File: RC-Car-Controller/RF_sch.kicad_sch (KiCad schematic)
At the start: 13 parts, among them U1 AT86RF215-ZU, U5 RFX2401C, U6 2450FB15A050E

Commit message: Fixed Controller PCB
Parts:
- C24, C25, C26, C27, C28, C29, C30, C31, C32, C33: footprint (none) -> Capacitor_SMD:C_0201_0603Metric
- U1: footprint QFN48_PQ_MCH -> footprints:QFN48_PQ_MCH
- U5: footprint RFX2401C_SKY -> footprints:RFX2401C_SKY
- U6: footprint 2450FB15A050E_JOT -> footprints:2450FB15A050E_JOT
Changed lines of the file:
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@@
 			)
 		)
-		(property "Footprint" "QFN48_PQ_MCH"
+		(property "Footprint" "footprints:QFN48_PQ_MCH"
 			(at 105.41 128.27 0)
 			(effects
@@
 			)
 		)
-		(property "Footprint" ""
+		(property "Footprint" "Capacitor_SMD:C_0201_0603Metric"
 			(at 267.6652 100.33 0)
 			(effects
@@
 			)
 		)
-		(property "Footprint" ""
+		(property "Footprint" "Capacitor_SMD:C_0201_0603Metric"
 			(at 101.2952 156.21 0)
 			(effects
@@
 			)
 		)
-		(property "Footprint" ""
+		(property "Footprint" "Capacitor_SMD:C_0201_0603Metric"
 			(at 59.3852 156.21 0)
 			(effects
@@
 			)
 		)
-		(property "Footprint" ""
+		(property "Footprint" "Capacitor_SMD:C_0201_0603Metric"
 			(at 77.1652 156.21 0)
 			(effects
@@
 			)
 		)
-		(property "Footprint" ""
+		(property "Footprint" "Capacitor_SMD:C_0201_0603Metric"
 			(at 93.6752 156.21 0)
 			(effects
@@
 			)
 		)
-		(property "Footprint" ""
+		(property "Footprint" "Capacitor_SMD:C_0201_0603Metric"
 			(at 108.9152 156.21 0)
 			(effects
@@
 			)
 		)
-		(property "Footprint" ""
+		(property "Footprint" "Capacitor_SMD:C_0201_0603Metric"
 			(at 271.4752 95.25 0)
 			(effects
@@
 			)
 		)
-		(property "Footprint" ""
+		(property "Footprint" "Capacitor_SMD:C_0201_0603Metric"
 			(at 86.0552 156.21 0)
 			(effects
@@
 			)
 		)
-		(property "Footprint" ""
+		(property "Footprint" "Capacitor_SMD:C_0201_0603Metric"
 			(at 68.2752 156.21 0)
 			(effects
@@
 			)
 		)
-		(property "Footprint" ""
+		(property "Footprint" "Capacitor_SMD:C_0201_0603Metric"
 			(at 50.4952 156.21 0)
 			(effects
@@
 			)
 		)
-		(property "Footprint" "2450FB15A050E_JOT"
+		(property "Footprint" "footprints:2450FB15A050E_JOT"
 			(at 121.92 87.63 0)
 			(effects
@@
 			)
 		)
-		(property "Footprint" "RFX2401C_SKY"
+		(property "Footprint" "footprints:RFX2401C_SKY"
 			(at 222.25 85.09 0)
 			(effects

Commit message: Did power schtuff
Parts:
- removed C24, C25, C26, C27, C28, C29, C30, C31, C32, C33: 0.1uF/10V, Capacitor_SMD:C_0201_0603Metric, symbol Device:C
- removed U1: AT86RF215-ZU, footprints:QFN48_PQ_MCH, symbol AT86RF215:AT86RF215-ZU
- removed U5: RFX2401C, footprints:RFX2401C_SKY, symbol RFX2401C:RFX2401C
- removed U6: 2450FB15A050E, footprints:2450FB15A050E_JOT, symbol 2450FB15A050E Balun:2450FB15A050E
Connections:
- no-connect marks 21 -> 0

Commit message: Added FGH100M footprint/schematic
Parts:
- added R26, R28, R29, R30, R31: 10k, Capacitor_SMD:C_0603_1608Metric, symbol Device:R
- added U3: ~, FGH100M:FGH100MABMD, symbol FGH100M:FGH100MABMD
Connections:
- new net +3V3: R26.2, R28.2, R29.2, R30.2, R31.2, U3.17 (VBAT), U3.22 (VDD_IO), U3.4 (VDD_FEM)
- new net GNDA: U3.1 (GND), U3.18 (GND), U3.2 (GND), U3.21 (GND), U3.3 (GND), U3.31 (GND), U3.38 (GND), U3.39 (GND), U3.5 (GND), U3.7 (GND)
- new net SDIO_CLK: U3.24 (SDIO_CLK)
- new net SDIO_CMD: R26.1, U3.23 (SDIO_CMD)
- new net SDIO_DATA0: R28.1, U3.25 (SDIO_DATA0)
- new net SDIO_DATA1: R29.1, U3.26 (SDIO_DATA1)
- new net SDIO_DATA2: R30.1, U3.19 (SDIO_DATA2)
- new net SDIO_DATA3: R31.1, U3.20 (SDIO_DATA3)
- no-connect marks 0 -> 12

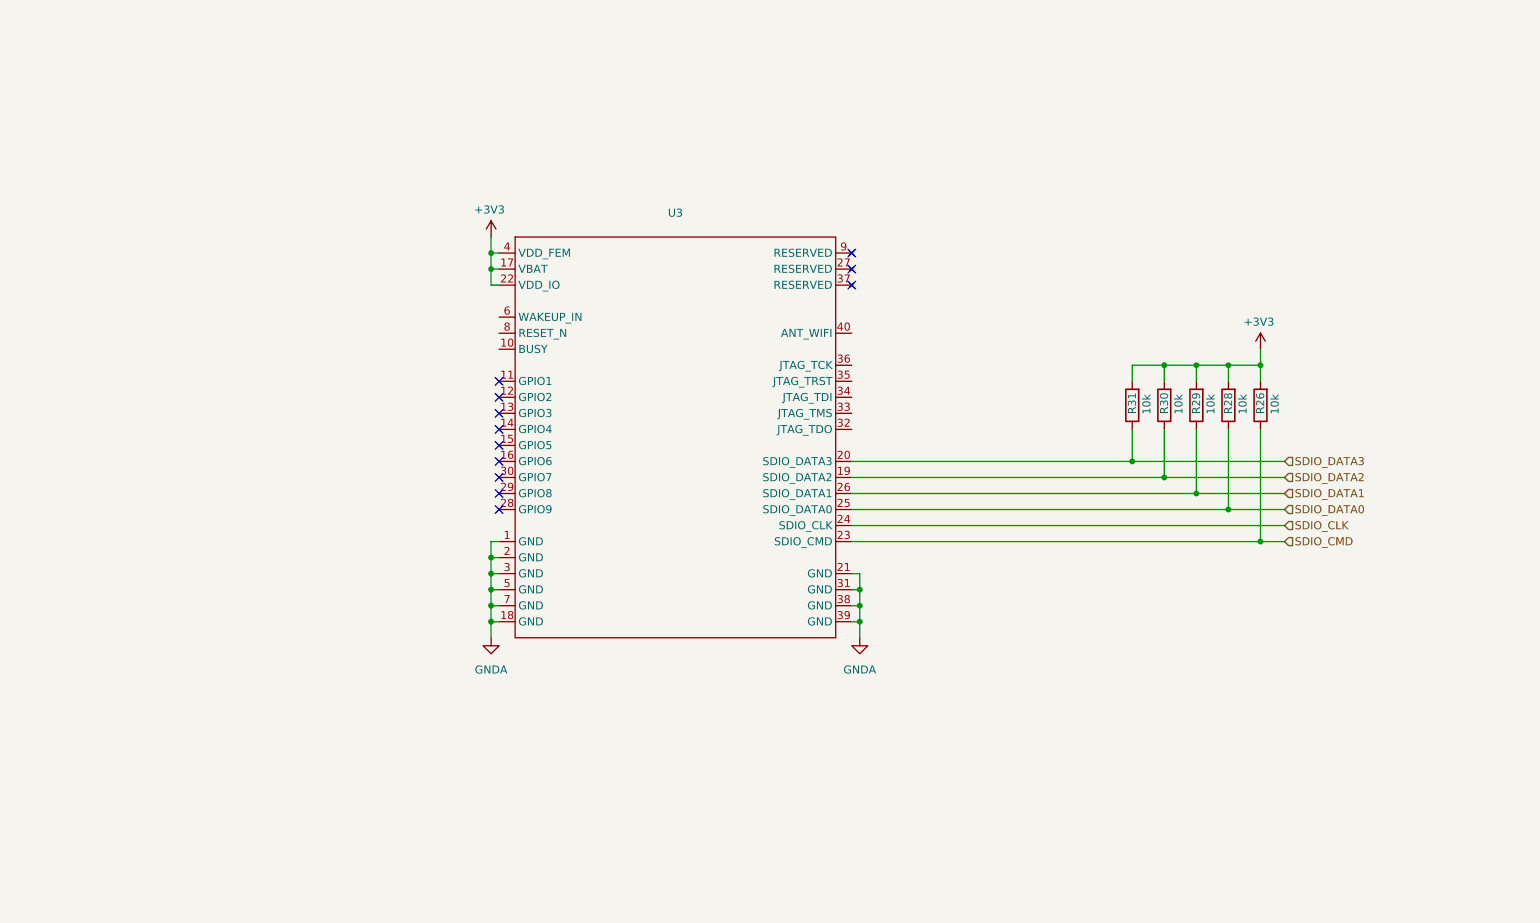
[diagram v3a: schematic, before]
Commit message: Wired up FGH100M
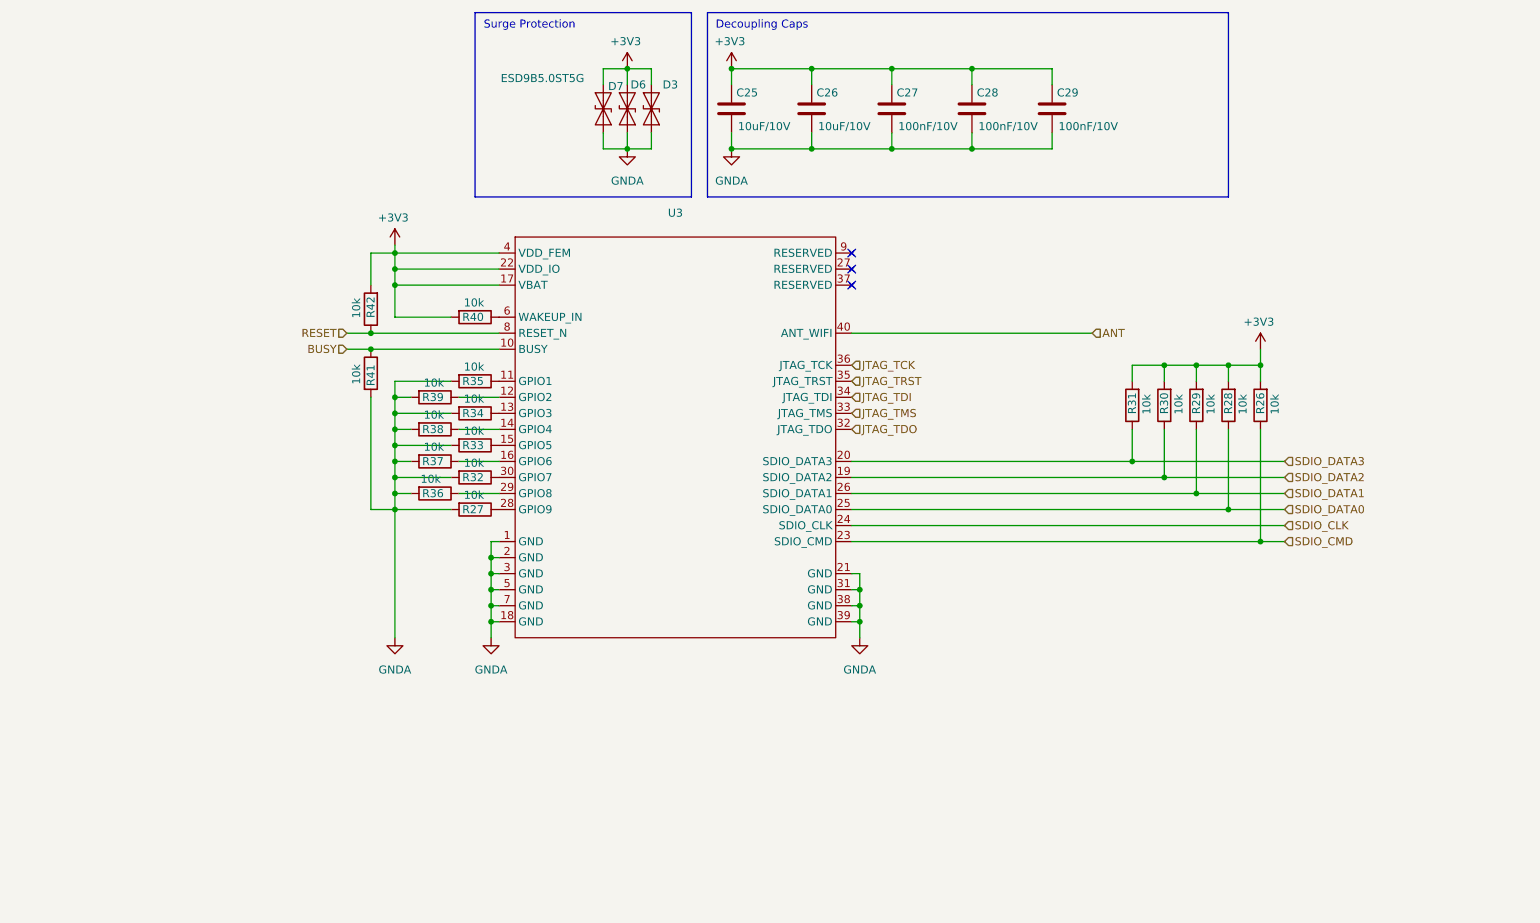
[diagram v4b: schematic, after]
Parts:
- added C25, C26: 10uF/10V, Capacitor_SMD:C_0603_1608Metric, symbol Device:C
- added C27, C28, C29: 100nF/10V, Capacitor_SMD:C_0603_1608Metric, symbol Device:C
- added D3, D6, D7: ESD9B5.0ST5G, Diode_SMD:D_SOD-923, symbol Diode:ESD9B5.0ST5G
- added R27, R32, R33, R34, R35, R36, R37, R38, R39, R40, R41, R42: 10k, Capacitor_SMD:C_0603_1608Metric, symbol Device:R
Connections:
- net +3V3: now also C25.1, C26.1, C27.1, C28.1, C29.1, D3.2 (A2), D6.2 (A2), D7.2 (A2), R40.2, R42.2
- net GNDA: now also C25.2, C26.2, C27.2, C28.2, C29.2, D3.1 (A1), D6.1 (A1), D7.1 (A1), R27.2, R32.2, R33.2, R34.2, R35.2, R36.2, R37.2, R38.2, R39.2, R41.2
- net BUSY: now reaches U3.10 (BUSY)
- net BUSY: now also R41.1
- net at U3.11 (GPIO1): now also R35.1
- net at U3.12 (GPIO2): now also R39.1
- net at U3.13 (GPIO3): now also R34.1
- net at U3.14 (GPIO4): now also R38.1
- net at U3.15 (GPIO5): now also R33.1
- net at U3.16 (GPIO6): now also R37.1
- net at U3.28 (GPIO9): now also R27.1
- net at U3.29 (GPIO8): now also R36.1
- net at U3.30 (GPIO7): now also R32.1
- net JTAG_TDO: now reaches U3.32 (JTAG_TDO)
- net JTAG_TMS: now reaches U3.33 (JTAG_TMS)
- net JTAG_TDI: now reaches U3.34 (JTAG_TDI)
- net JTAG_TRST: now reaches U3.35 (JTAG_TRST)
- net JTAG_TCK: now reaches U3.36 (JTAG_TCK)
- net ANT: now reaches U3.40 (ANT_WIFI)
- net at U3.6 (WAKEUP_IN): now also R40.1
- net RESET: now reaches U3.8 (RESET_N)
- net RESET: now also R42.1
- no-connect marks 12 -> 3
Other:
- note added: "Decoupling Caps"
- note added: "Surge Protection"

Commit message: Finished Controller PCB Pre-Review
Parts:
- added C26, C28: DNP, Capacitor_SMD:C_0603_1608Metric, symbol Device:C
- added FB1: FerriteBead, Capacitor_SMD:C_0603_1608Metric, symbol Device:FerriteBead
- added R35, R36, R37, R39: 10k, Capacitor_SMD:C_0603_1608Metric, symbol Device:R
- added R38: 0ohm, Resistor_SMD:R_0603_1608Metric, symbol Device:R
- D6: renamed from D7; now not fitted; now left out of the parts list
- D7: renamed from D6; now not fitted; now left out of the parts list
- D8: renamed from D3; now not fitted; now left out of the parts list
- renumbered C26 to C23, C29 to C24, C28 to C25, C25 to C27, C27 to C29, R42 to R23, R41 to R24, R39 to R25, R38 to R26, R37 to R27, R36 to R28, R40 to R29, R35 to R30, R34 to R31, R33 to R32, R32 to R33, R27 to R34, R31 to R40, R30 to R41, R29 to R42, R28 to R43, R26 to R44, U3 to U6
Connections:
- net +3V3: now also FB1.1; no longer C27.1, C29.1, U6.4 (VDD_FEM)
- net ANT: now also C28.1, R38.1; no longer U6.40 (ANT_WIFI)
- net GNDA: now also C26.2, C28.2, R35.1, R36.1, R37.1, R39.1
- net JTAG_TCK: now also R39.2
- net JTAG_TDI: now also R37.2
- net JTAG_TDO: now also R35.2
- net JTAG_TMS: now also R36.2
- new net: C26.1, R38.2, U6.40 (ANT_WIFI)
- new net VDD_FEM: C27.1, C29.1, FB1.2, U6.4 (VDD_FEM)
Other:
- moved on the sheet: C23, C24, C25, C27, C29

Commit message: most resistors given PNs
most resistors given PNs. some remaining
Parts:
- R23, R24, R25, R26, R27, R28, R29, R30, R31, R32, R33, R34, R35, R36, R37, R39, R40, R41, R42, R43, R44: MANUF_PN (none) -> RC0603FR-0710KL
- R38: MANUF_PN (none) -> RMCF0603ZT0R00

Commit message: controller cpnts given MANUF_PNs
controller cpnts given MANUF_PNs. not all components, but all resistors are done
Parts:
- D6, D7, D8: MANUF_PN (none) -> ESD9B5.0ST5G
- FB1: MANUF_PN (none) -> HCB 1608KF-181T20
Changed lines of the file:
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@@
 			)
 		)
-		(property "MANUF_PN" ""
+		(property "MANUF_PN" "ESD9B5.0ST5G"
 			(at 147.32 35.56 0)
 			(effects
@@
 			)
 		)
-		(property "MANUF_PN" ""
+		(property "MANUF_PN" "ESD9B5.0ST5G"
 			(at 139.7 35.56 0)
 			(effects
@@
 			)
 		)
-		(property "MANUF_PN" ""
+		(property "MANUF_PN" "ESD9B5.0ST5G"
 			(at 143.51 35.56 0)
 			(effects
@@
 			)
 		)
-		(property "MANUF_PN" ""
+		(property "MANUF_PN" "HCB 1608KF-181T20"
 			(at 196.85 29.21 0)
 			(effects

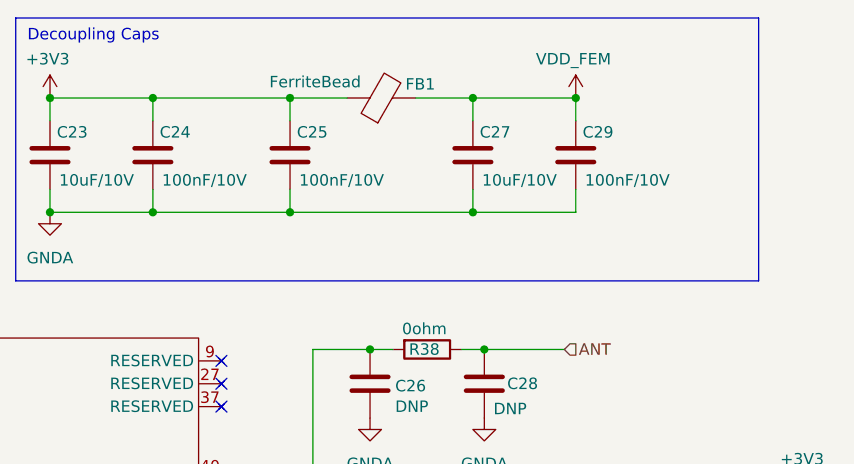
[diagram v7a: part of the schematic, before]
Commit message: Filled out some Controller Caps
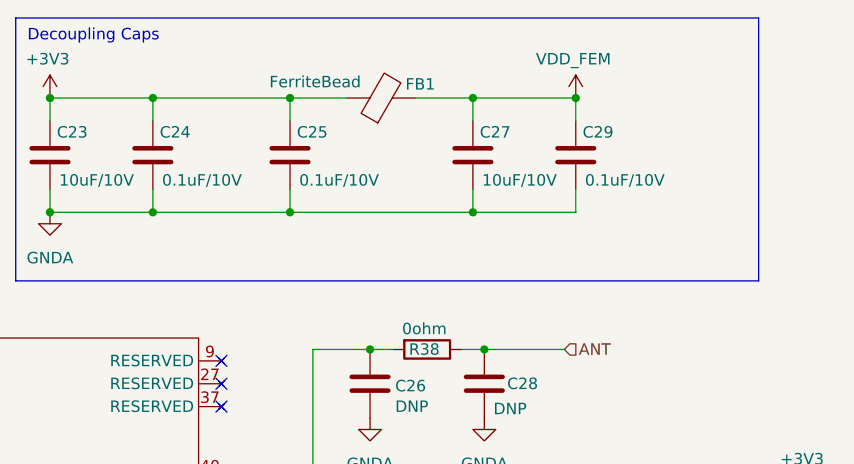
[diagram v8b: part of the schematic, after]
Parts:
- C24, C25, C29: value 100nF/10V -> 0.1uF/10V; MANUF_PN (none) -> C0603C104K5RAC7411
- C26, C28: MANUF_PN (none) -> N/A
- U6: MANUF_PN (none) -> FGH100MABMD
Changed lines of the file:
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@@
 			)
 		)
-		(property "Value" "100nF/10V"
+		(property "Value" "0.1uF/10V"
 			(at 172.466 38.354 0)
 			(effects
@@
 			)
 		)
-		(property "MANUF_PN" ""
+		(property "MANUF_PN" "C0603C104K5RAC7411"
 			(at 171.45 35.56 0)
 			(effects
@@
 			)
 		)
-		(property "Value" "100nF/10V"
+		(property "Value" "0.1uF/10V"
 			(at 219.456 38.354 0)
 			(effects
@@
 			)
 		)
-		(property "MANUF_PN" ""
+		(property "MANUF_PN" "C0603C104K5RAC7411"
 			(at 218.44 35.56 0)
 			(effects
@@
 			)
 		)
-		(property "MANUF_PN" ""
+		(property "MANUF_PN" "FGH100MABMD"
 			(at 151.13 88.9 0)
 			(effects
@@
 			)
 		)
-		(property "MANUF_PN" ""
+		(property "MANUF_PN" "N/A"
 			(at 208.28 60.96 0)
 			(effects
@@
 			)
 		)
-		(property "Value" "100nF/10V"
+		(property "Value" "0.1uF/10V"
 			(at 187.706 38.354 0)
 			(effects
@@
 			)
 		)
-		(property "MANUF_PN" ""
+		(property "MANUF_PN" "C0603C104K5RAC7411"
 			(at 186.69 35.56 0)
 			(effects
@@
 			)
 		)
-		(property "MANUF_PN" ""
+		(property "MANUF_PN" "N/A"
 			(at 195.58 60.96 0)
 			(effects
